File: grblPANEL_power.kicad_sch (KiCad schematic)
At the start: 27 parts, among them J101 Conn_01x02, U101 MAX17612A, U102 AZ1117-3.3

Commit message: PCB layout - WIP
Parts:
- J101: footprint TerminalBlock_4Ucon:TerminalBlock_4Ucon_1x02_P3.50mm_Horizontal -> TerminalBlock_Phoenix:TerminalBlock_Phoenix_PT-1,5-2-3.5-H_1x02_P3.50mm_Horizontal
- TP101: footprint Connector_Pin:Pin_D1.0mm_L10.0mm_LooseFit -> TestPoint:TestPoint_THTPad_D2.0mm_Drill1.0mm
- TP102, TP103, TP104, TP105: footprint Connector_Pin:Pin_D1.0mm_L10.0mm -> TestPoint:TestPoint_THTPad_D2.0mm_Drill1.0mm
- U101: footprint Package_DFN_QFN:TDFN-10-1EP_2x3mm_P0.5mm_EP0.9x2mm_ThermalVias -> dresco:TDFN-10-1EP_3x3mm_P0.5mm_EP1.6x2.39mm_ThermalVias
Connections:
- net GND: now also J101.2 (Pin_2), U101.11 (GND); no longer J101.1 (Pin_1)
- net VIN: now also J101.1 (Pin_1); no longer J101.2 (Pin_2)
- net SETI: now reaches R106.1, U101.8 (SETI)
- net ULVO: now reaches R101.2, R102.1, U101.2 (UVLO)
- net FLAG: now reaches TP102.1, U101.6 (~{FLAG})
- net OVLO: now reaches R103.2, R104.1, U101.3 (OVLO)
- net VIN_PROT: now reaches C102.1, R108.1, U101.10 (OUT)
- net VIN_PI_OUT: now reaches C104.1, C105.1, L101.2, U102.3 (VI)
- net UVOV: now reaches TP103.1, U101.7 (~{UVOV})
- net VIN_PI_IN: now reaches C103.1, D102.1 (K), L101.1, R107.2, R108.2
- net CLMODE: now reaches R105.1, U101.4 (CLMODE)
- net PWR_LED_K: now reaches D103.1 (K), R109.1
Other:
- moved on the sheet: J101, R109, TP102, TP103
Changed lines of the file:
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@@
     (company "dresco")
   )
-  (junction (at 106.68 95.25) (diameter 0) (color 0 0 0 0)
+  (junction (at 105.41 95.25) (diameter 0) (color 0 0 0 0)
   )
   (junction (at 46.99 64.77) (diameter 0) (color 0 0 0 0)
@@
   )
   (junction (at 91.44 64.77) (diameter 0) (color 0 0 0 0)
+  )
+  (junction (at 105.41 91.44) (diameter 0) (color 0 0 0 0)
   )
   (junction (at 77.47 95.25) (diameter 0) (color 0 0 0 0)
@@
     (stroke (width 0) (type default) (color 0 0 0 0))
   )
-  (wire (pts (xy 119.38 77.47) (xy 120.65 77.47))
+  (wire (pts (xy 119.38 77.47) (xy 134.62 77.47))
     (stroke (width 0) (type default) (color 0 0 0 0))
   )
@@
     (stroke (width 0) (type default) (color 0 0 0 0))
   )
+  (wire (pts (xy 107.95 91.44) (xy 105.41 91.44))
+    (stroke (width 0) (type default) (color 0 0 0 0))
+  )
   (wire (pts (xy 161.29 62.23) (xy 161.29 64.77))
     (stroke (width 0) (type default) (color 0 0 0 0))
@@
     (stroke (width 0) (type default) (color 0 0 0 0))
   )
-  (wire (pts (xy 119.38 80.01) (xy 120.65 80.01))
+  (wire (pts (xy 119.38 80.01) (xy 134.62 80.01))
     (stroke (width 0) (type default) (color 0 0 0 0))
   )
@@
     (stroke (width 0) (type default) (color 0 0 0 0))
   )
-  (wire (pts (xy 106.68 90.17) (xy 106.68 95.25))
+  (wire (pts (xy 105.41 90.17) (xy 105.41 91.44))
     (stroke (width 0) (type default) (color 0 0 0 0))
   )
@@
     (stroke (width 0) (type default) (color 0 0 0 0))
   )
-  (wire (pts (xy 248.92 76.2) (xy 248.92 83.82))
+  (wire (pts (xy 248.92 76.2) (xy 248.92 86.36))
     (stroke (width 0) (type default) (color 0 0 0 0))
   )
@@
     (stroke (width 0) (type default) (color 0 0 0 0))
   )
-  (wire (pts (xy 248.92 91.44) (xy 248.92 95.25))
+  (wire (pts (xy 248.92 93.98) (xy 248.92 95.25))
     (stroke (width 0) (type default) (color 0 0 0 0))
   )
@@
     (stroke (width 0) (type default) (color 0 0 0 0))
   )
+  (wire (pts (xy 107.95 90.17) (xy 107.95 91.44))
+    (stroke (width 0) (type default) (color 0 0 0 0))
+  )
   (wire (pts (xy 180.34 95.25) (xy 185.42 95.25))
     (stroke (width 0) (type default) (color 0 0 0 0))
@@
     (stroke (width 0) (type default) (color 0 0 0 0))
   )
-  (wire (pts (xy 87.63 95.25) (xy 106.68 95.25))
+  (wire (pts (xy 87.63 95.25) (xy 105.41 95.25))
     (stroke (width 0) (type default) (color 0 0 0 0))
   )
@@
     (stroke (width 0) (type default) (color 0 0 0 0))
   )
+  (wire (pts (xy 105.41 91.44) (xy 105.41 95.25))
+    (stroke (width 0) (type default) (color 0 0 0 0))
+  )
   (polyline (pts (xy 194.31 100.33) (xy 194.31 120.65))
     (stroke (width 0) (type default) (color 0 0 0 0))
@@
     (stroke (width 0) (type default) (color 0 0 0 0))
   )
-  (wire (pts (xy 106.68 95.25) (xy 128.27 95.25))
+  (wire (pts (xy 105.41 95.25) (xy 128.27 95.25))
     (stroke (width 0) (type default) (color 0 0 0 0))
   )
@@
     (effects (font (size 1.27 1.27)) (justify left bottom))
   )
+  (label "UVOV" (at 130.81 80.01 0)
+    (effects (font (size 1.27 1.27)) (justify left bottom))
+  )
+  (label "PWR_LED_K" (at 248.92 76.2 270)
+    (effects (font (size 1.27 1.27)) (justify right bottom))
+  )
+  (label "FLAG" (at 130.81 77.47 0)
+    (effects (font (size 1.27 1.27)) (justify left bottom))
+  )
+  (label "ULVO" (at 86.36 82.55 0)
+    (effects (font (size 1.27 1.27)) (justify left bottom))
+  )
+  (label "VIN_PI_IN" (at 166.37 64.77 0)
+    (effects (font (size 1.27 1.27)) (justify left bottom))
+  )
+  (label "OVLO" (at 86.36 80.01 0)
+    (effects (font (size 1.27 1.27)) (justify left bottom))
+  )
+  (label "CLMODE" (at 93.98 85.09 180)
+    (effects (font (size 1.27 1.27)) (justify right bottom))
+  )
+  (label "VIN_PROT" (at 120.65 64.77 0)
+    (effects (font (size 1.27 1.27)) (justify left bottom))
+  )
+  (label "SETI" (at 123.19 85.09 0)
+    (effects (font (size 1.27 1.27)) (justify left bottom))
+  )
+  (label "VIN_PI_OUT" (at 193.04 64.77 0)
+    (effects (font (size 1.27 1.27)) (justify left bottom))
+  )
   (symbol (lib_id "Device:R") (at 128.27 90.17 0) (unit 1)
     (in_bom yes) (on_board yes) (fields_autoplaced)
@@
     (pin "2")
   )
-  (symbol (lib_id "Connector_Generic:Conn_01x02") (at 35.56 67.31 180) (unit 1)
+  (symbol (lib_id "Connector_Generic:Conn_01x02") (at 35.56 64.77 0) (mirror y) (unit 1)
     (in_bom yes) (on_board yes) (fields_autoplaced)
     (property "Reference" "J101" (id 0) (at 35.56 58.42 0))
     (property "Value" "Conn_01x02" (id 1) (at 35.56 60.96 0))
-    (property "Footprint" "TerminalBlock_4Ucon:TerminalBlock_4Ucon_1x02_P3.50mm_Horizontal" (id 2) (at 35.56 67.31 0)
-      (effects (font (size 1.27 1.27)) hide)
-    )
-    (property "Datasheet" "~" (id 3) (at 35.56 67.31 0)
+    (property "Footprint" "TerminalBlock_Phoenix:TerminalBlock_Phoenix_PT-1,5-2-3.5-H_1x02_P3.50mm_Horizontal" (id 2) (at 35.56 64.77 0)
+      (effects (font (size 1.27 1.27)) hide)
+    )
+    (property "Datasheet" "~" (id 3) (at 35.56 64.77 0)
       (effects (font (size 1.27 1.27)) hide)
     )
@@
       (effects (font (size 1.27 1.27)) (justify left) hide)
     )
-    (property "Footprint" "Connector_Pin:Pin_D1.0mm_L10.0mm" (id 2) (at 190.5 95.25 0)
+    (property "Footprint" "TestPoint:TestPoint_THTPad_D2.0mm_Drill1.0mm" (id 2) (at 190.5 95.25 0)
       (effects (font (size 1.27 1.27)) hide)
     )
@@
     (pin "2")
   )
-  (symbol (lib_id "Connector:TestPoint") (at 120.65 77.47 270) (unit 1)
-    (in_bom yes) (on_board yes)
-    (property "Reference" "TP102" (id 0) (at 124.46 78.74 90)
-      (effects (font (size 1.27 1.27)) (justify left))
-    )
-    (property "Value" "TestPoint" (id 1) (at 125.73 77.47 90)
+  (symbol (lib_id "Connector:TestPoint") (at 134.62 77.47 270) (unit 1)
+    (in_bom yes) (on_board yes)
+    (property "Reference" "TP102" (id 0) (at 138.43 78.74 90)
+      (effects (font (size 1.27 1.27)) (justify left))
+    )
+    (property "Value" "TestPoint" (id 1) (at 139.7 77.47 90)
       (effects (font (size 1.27 1.27)) (justify left) hide)
     )
-    (property "Footprint" "Connector_Pin:Pin_D1.0mm_L10.0mm" (id 2) (at 120.65 82.55 0)
-      (effects (font (size 1.27 1.27)) hide)
-    )
-    (property "Datasheet" "~" (id 3) (at 120.65 82.55 0)
+    (property "Footprint" "TestPoint:TestPoint_THTPad_D2.0mm_Drill1.0mm" (id 2) (at 134.62 82.55 0)
+      (effects (font (size 1.27 1.27)) hide)
+    )
+    (property "Datasheet" "~" (id 3) (at 134.62 82.55 0)
       (effects (font (size 1.27 1.27)) hide)
     )
@@
     (pin "1")
   )
-  (symbol (lib_id "Connector:TestPoint") (at 120.65 80.01 270) (unit 1)
-    (in_bom yes) (on_board yes)
-    (property "Reference" "TP103" (id 0) (at 124.46 81.28 90)
-      (effects (font (size 1.27 1.27)) (justify left))
-    )
-    (property "Value" "TestPoint" (id 1) (at 125.73 80.01 90)
+  (symbol (lib_id "Connector:TestPoint") (at 134.62 80.01 270) (unit 1)
+    (in_bom yes) (on_board yes)
+    (property "Reference" "TP103" (id 0) (at 138.43 81.28 90)
+      (effects (font (size 1.27 1.27)) (justify left))
+    )
+    (property "Value" "TestPoint" (id 1) (at 139.7 80.01 90)
       (effects (font (size 1.27 1.27)) (justify left) hide)
     )
-    (property "Footprint" "Connector_Pin:Pin_D1.0mm_L10.0mm" (id 2) (at 120.65 85.09 0)
-      (effects (font (size 1.27 1.27)) hide)
-    )
-    (property "Datasheet" "~" (id 3) (at 120.65 85.09 0)
+    (property "Footprint" "TestPoint:TestPoint_THTPad_D2.0mm_Drill1.0mm" (id 2) (at 134.62 85.09 0)
+      (effects (font (size 1.27 1.27)) hide)
+    )
+    (property "Datasheet" "~" (id 3) (at 134.62 85.09 0)
       (effects (font (size 1.27 1.27)) hide)
     )
@@
     (property "Reference" "U101" (id 0) (at 106.68 58.42 0))
     (property "Value" "MAX17612A" (id 1) (at 106.68 60.96 0))
-    (property "Footprint" "Package_DFN_QFN:TDFN-10-1EP_2x3mm_P0.5mm_EP0.9x2mm_ThermalVias" (id 2) (at 106.68 74.93 0)
+    (property "Footprint" "dresco:TDFN-10-1EP_3x3mm_P0.5mm_EP1.6x2.39mm_ThermalVias" (id 2) (at 106.68 74.93 0)
       (effects (font (size 1.27 1.27)) hide)
     )
@@
     (pin "1")
     (pin "10")
+    (pin "11")
     (pin "2")
     (pin "3")
@@
       (effects (font (size 1.27 1.27)) (justify left) hide)
     )
-    (property "Footprint" "Connector_Pin:Pin_D1.0mm_L10.0mm_LooseFit" (id 2) (at 55.88 64.77 0)
+    (property "Footprint" "TestPoint:TestPoint_THTPad_D2.0mm_Drill1.0mm" (id 2) (at 55.88 64.77 0)
       (effects (font (size 1.27 1.27)) hide)
     )
@@
       (effects (font (size 1.27 1.27)) (justify left) hide)
     )
-    (property "Footprint" "Connector_Pin:Pin_D1.0mm_L10.0mm" (id 2) (at 257.81 64.77 0)
+    (property "Footprint" "TestPoint:TestPoint_THTPad_D2.0mm_Drill1.0mm" (id 2) (at 257.81 64.77 0)
       (effects (font (size 1.27 1.27)) hide)
     )
@@
     (pin "2")
   )
-  (symbol (lib_id "Device:R") (at 248.92 87.63 0) (unit 1)
-    (in_bom yes) (on_board yes) (fields_autoplaced)
-    (property "Reference" "R109" (id 0) (at 251.46 86.3599 0)
-      (effects (font (size 1.27 1.27)) (justify left))
-    )
-    (property "Value" "1k" (id 1) (at 251.46 88.8999 0)
-      (effects (font (size 1.27 1.27)) (justify left))
-    )
-    (property "Footprint" "Resistor_SMD:R_0603_1608Metric" (id 2) (at 247.142 87.63 90)
-      (effects (font (size 1.27 1.27)) hide)
-    )
-    (property "Datasheet" "~" (id 3) (at 248.92 87.63 0)
-      (effects (font (size 1.27 1.27)) hide)
-    )
+  (symbol (lib_id "Device:R") (at 248.92 90.17 0) (unit 1)
+    (in_bom yes) (on_board yes) (fields_autoplaced)
+    (property "Reference" "R109" (id 0) (at 251.46 88.8999 0)
+      (effects (font (size 1.27 1.27)) (justify left))
+    )
+    (property "Value" "1k" (id 1) (at 251.46 91.4399 0)
+      (effects (font (size 1.27 1.27)) (justify left))
+    )
+    (property "Footprint" "Resistor_SMD:R_0603_1608Metric" (id 2) (at 247.142 90.17 90)
+      (effects (font (size 1.27 1.27)) hide)
+    )
+    (property "Datasheet" "~" (id 3) (at 248.92 90.17 0)
+      (effects (font (size 1.27 1.27)) hide)
+    )

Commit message: power section cleanup change 1206 caps to 0805
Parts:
- C102, C105, C106: footprint Capacitor_SMD:C_1206_3216Metric -> Capacitor_SMD:C_0805_2012Metric
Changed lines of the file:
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@@
       (effects (font (size 1.27 1.27)) (justify left))
     )
-    (property "Footprint" "Capacitor_SMD:C_1206_3216Metric" (id 2) (at 127.9652 73.66 0)
+    (property "Footprint" "Capacitor_SMD:C_0805_2012Metric" (id 2) (at 127.9652 73.66 0)
       (effects (font (size 1.27 1.27)) hide)
     )
@@
       (effects (font (size 1.27 1.27)) (justify left))
     )
-    (property "Footprint" "Capacitor_SMD:C_1206_3216Metric" (id 2) (at 229.5652 83.82 0)
+    (property "Footprint" "Capacitor_SMD:C_0805_2012Metric" (id 2) (at 229.5652 83.82 0)
       (effects (font (size 1.27 1.27)) hide)
     )
@@
       (effects (font (size 1.27 1.27)) (justify left))
     )
-    (property "Footprint" "Capacitor_SMD:C_1206_3216Metric" (id 2) (at 206.7052 83.82 0)
-      (effects (font (size 1.27 1.27)) hide)
-    )
+    (property "Footprint" "Capacitor_SMD:C_0805_2012Metric" (id 2) (at 206.7052 83.82 0)
+      (effects (font (size 1.27 1.27)) hide)
+    )

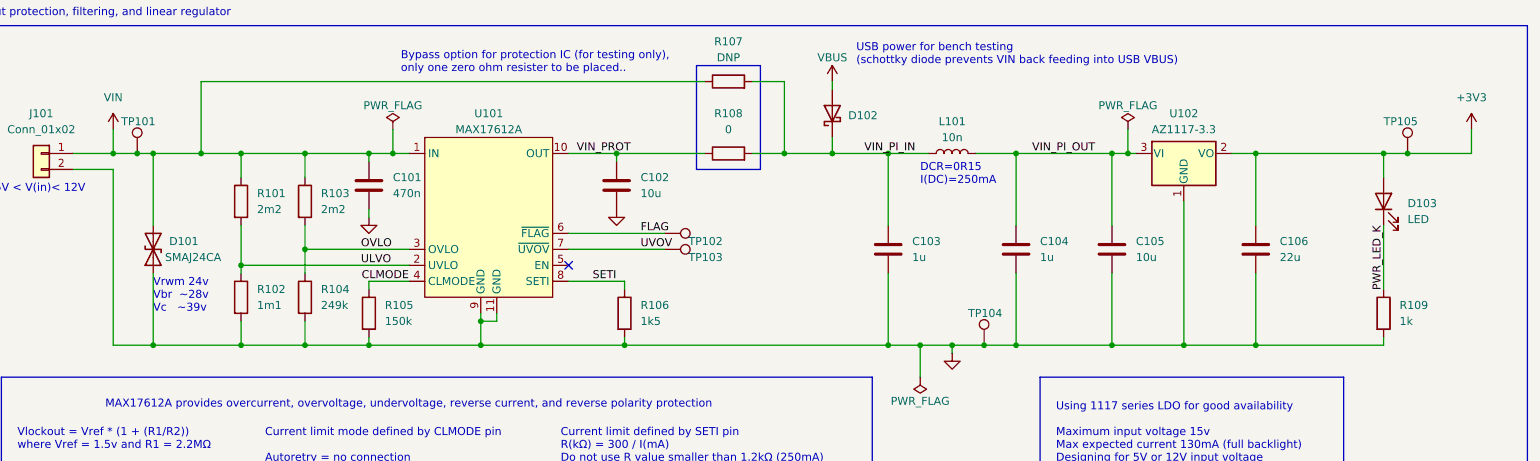
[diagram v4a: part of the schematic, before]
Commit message: sheet 1 test points
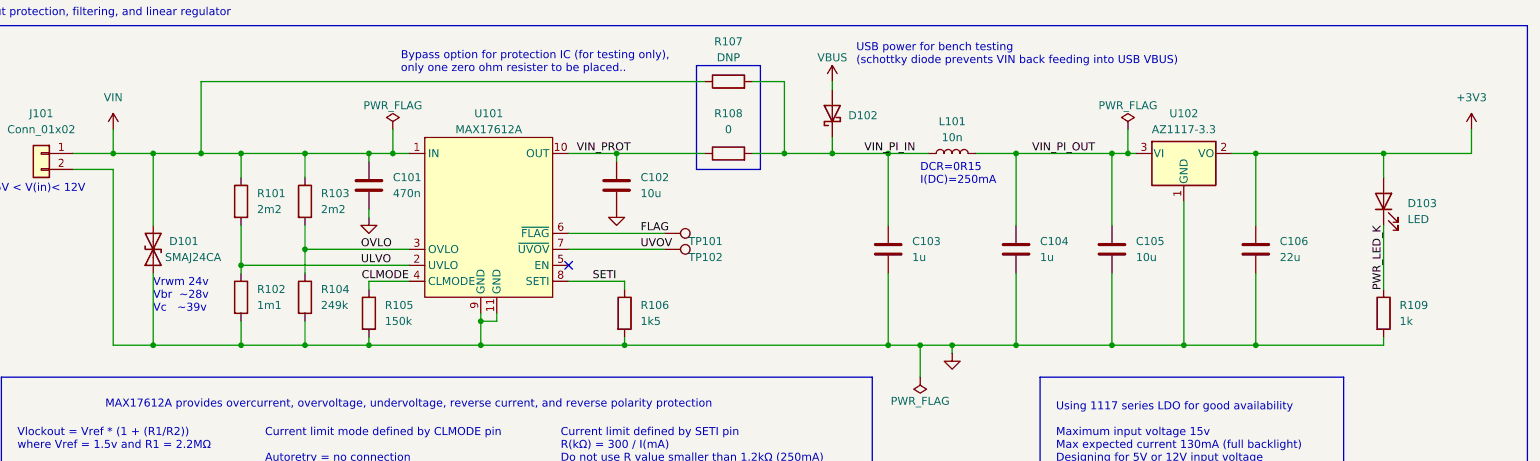
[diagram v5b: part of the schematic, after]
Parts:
- removed TP101, TP104, TP105: TestPoint, TestPoint:TestPoint_THTPad_D2.0mm_Drill1.0mm, symbol Connector:TestPoint
- renumbered TP102 to TP101, TP103 to TP102
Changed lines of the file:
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@@
   (junction (at 77.47 80.01) (diameter 0) (color 0 0 0 0)
   )
-  (junction (at 185.42 95.25) (diameter 0) (color 0 0 0 0)
-  )
   (junction (at 91.44 64.77) (diameter 0) (color 0 0 0 0)
   )
@@
   (junction (at 53.34 95.25) (diameter 0) (color 0 0 0 0)
   )
-  (junction (at 50.8 64.77) (diameter 0) (color 0 0 0 0)
-  )
   (junction (at 180.34 95.25) (diameter 0) (color 0 0 0 0)
   )
@@
   )
   (junction (at 205.74 64.77) (diameter 0) (color 0 0 0 0)
-  )
-  (junction (at 252.73 64.77) (diameter 0) (color 0 0 0 0)
   )
   (junction (at 77.47 64.77) (diameter 0) (color 0 0 0 0)
@@
     (stroke (width 0) (type default) (color 0 0 0 0))
   )
-  (wire (pts (xy 185.42 95.25) (xy 190.5 95.25))
-    (stroke (width 0) (type default) (color 0 0 0 0))
-  )
   (wire (pts (xy 119.38 64.77) (xy 127 64.77))
     (stroke (width 0) (type default) (color 0 0 0 0))
@@
     (stroke (width 0) (type default) (color 0 0 0 0))
   )
-  (wire (pts (xy 50.8 64.77) (xy 53.34 64.77))
+  (wire (pts (xy 46.99 64.77) (xy 53.34 64.77))
     (stroke (width 0) (type default) (color 0 0 0 0))
   )
@@
     (stroke (width 0) (type default) (color 0 0 0 0))
   )
-  (wire (pts (xy 46.99 64.77) (xy 50.8 64.77))
-    (stroke (width 0) (type default) (color 0 0 0 0))
-  )
   (polyline (pts (xy 149.86 50.8) (xy 149.86 67.31))
     (stroke (width 0) (type default) (color 0 0 0 0))
@@
     (stroke (width 0) (type default) (color 0 0 0 0))
   )
-  (wire (pts (xy 262.89 64.77) (xy 252.73 64.77))
-    (stroke (width 0) (type default) (color 0 0 0 0))
-  )
   (wire (pts (xy 77.47 95.25) (xy 87.63 95.25))
     (stroke (width 0) (type default) (color 0 0 0 0))
@@
     (stroke (width 0) (type default) (color 0 0 0 0))
   )
-  (wire (pts (xy 252.73 64.77) (xy 248.92 64.77))
+  (wire (pts (xy 248.92 64.77) (xy 262.89 64.77))
     (stroke (width 0) (type default) (color 0 0 0 0))
   )
@@
     (stroke (width 0) (type default) (color 0 0 0 0))
   )
-  (wire (pts (xy 180.34 95.25) (xy 185.42 95.25))
+  (wire (pts (xy 180.34 95.25) (xy 190.5 95.25))
     (stroke (width 0) (type default) (color 0 0 0 0))
   )
@@
     (pin "2")
   )
-  (symbol (lib_id "Connector:TestPoint") (at 185.42 95.25 0) (unit 1)
-    (in_bom yes) (on_board yes)
-    (property "Reference" "TP104" (id 0) (at 182.88 90.17 0)
-      (effects (font (size 1.27 1.27)) (justify left))
-    )
-    (property "Value" "TestPoint" (id 1) (at 185.42 90.17 90)
-      (effects (font (size 1.27 1.27)) (justify left) hide)
-    )
-    (property "Footprint" "TestPoint:TestPoint_THTPad_D2.0mm_Drill1.0mm" (id 2) (at 190.5 95.25 0)
-      (effects (font (size 1.27 1.27)) hide)
-    )
-    (property "Datasheet" "~" (id 3) (at 190.5 95.25 0)
-      (effects (font (size 1.27 1.27)) hide)
-    )
-    (pin "1")
-  )
   (symbol (lib_id "Device:R") (at 67.31 72.39 0) (unit 1)
     (in_bom yes) (on_board yes) (fields_autoplaced)
@@
   (symbol (lib_id "Connector:TestPoint") (at 134.62 77.47 270) (unit 1)
     (in_bom yes) (on_board yes)
-    (property "Reference" "TP102" (id 0) (at 138.43 78.74 90)
+    (property "Reference" "TP101" (id 0) (at 138.43 78.74 90)
       (effects (font (size 1.27 1.27)) (justify left))
     )
@@
   (symbol (lib_id "Connector:TestPoint") (at 134.62 80.01 270) (unit 1)
     (in_bom yes) (on_board yes)
-    (property "Reference" "TP103" (id 0) (at 138.43 81.28 90)
+    (property "Reference" "TP102" (id 0) (at 138.43 81.28 90)
       (effects (font (size 1.27 1.27)) (justify left))
     )
@@
     (pin "2")
   )
-  (symbol (lib_id "Connector:TestPoint") (at 50.8 64.77 0) (unit 1)
-    (in_bom yes) (on_board yes)
-    (property "Reference" "TP101" (id 0) (at 48.26 59.69 0)
-      (effects (font (size 1.27 1.27)) (justify left))
-    )
-    (property "Value" "TestPoint" (id 1) (at 50.8 59.69 90)
-      (effects (font (size 1.27 1.27)) (justify left) hide)
-    )
-    (property "Footprint" "TestPoint:TestPoint_THTPad_D2.0mm_Drill1.0mm" (id 2) (at 55.88 64.77 0)
-      (effects (font (size 1.27 1.27)) hide)
-    )
-    (property "Datasheet" "~" (id 3) (at 55.88 64.77 0)
-      (effects (font (size 1.27 1.27)) hide)
-    )
-    (pin "1")
-  )
   (symbol (lib_id "Device:C") (at 228.6 80.01 0) (unit 1)
     (in_bom yes) (on_board yes) (fields_autoplaced)
@@
     (pin "2")
   )
-  (symbol (lib_id "Connector:TestPoint") (at 252.73 64.77 0) (unit 1)
-    (in_bom yes) (on_board yes)
-    (property "Reference" "TP105" (id 0) (at 248.92 59.69 0)
-      (effects (font (size 1.27 1.27)) (justify left))
-    )
-    (property "Value" "TestPoint" (id 1) (at 252.73 59.69 90)
-      (effects (font (size 1.27 1.27)) (justify left) hide)
-    )
-    (property "Footprint" "TestPoint:TestPoint_THTPad_D2.0mm_Drill1.0mm" (id 2) (at 257.81 64.77 0)
-      (effects (font (size 1.27 1.27)) hide)
-    )
-    (property "Datasheet" "~" (id 3) (at 257.81 64.77 0)
-      (effects (font (size 1.27 1.27)) hide)
-    )
-    (pin "1")
-  )
   (symbol (lib_id "Device:D_TVS") (at 53.34 80.01 90) (unit 1)

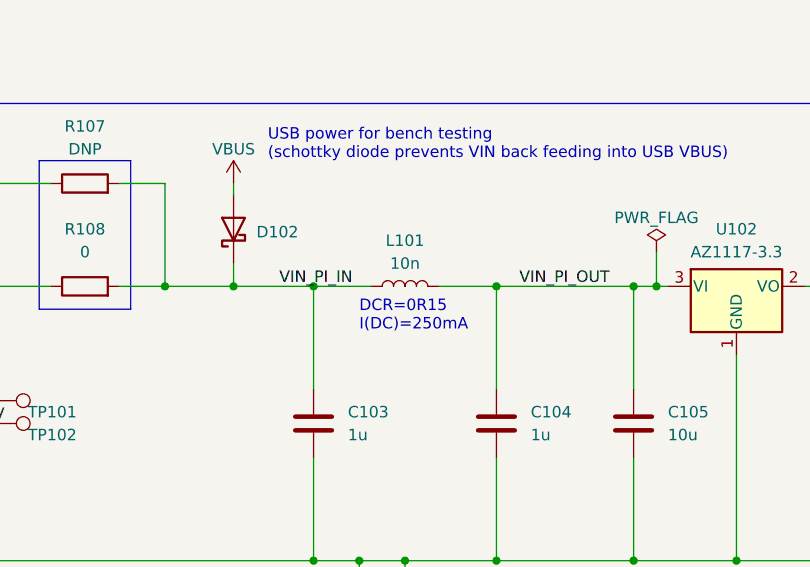
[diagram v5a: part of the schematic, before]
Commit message: v7 upgrade
schematic symbols updated from libraries

pcb update from schematic
update footprints from library

board setup, thermal relief count

still DRC warnings where symbols have been updated locally with 3d
models etc

copper sliver warning from zone fill
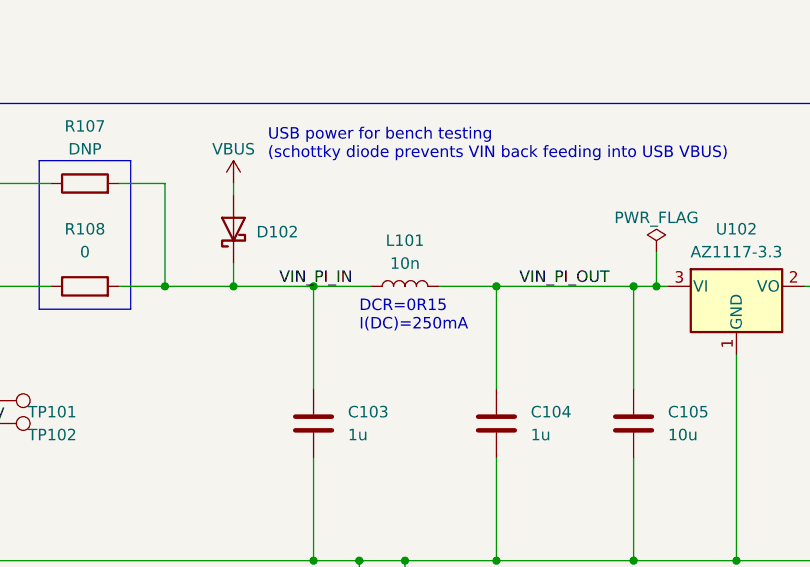
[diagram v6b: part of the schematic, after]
